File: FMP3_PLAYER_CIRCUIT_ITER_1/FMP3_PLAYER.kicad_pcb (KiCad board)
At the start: 4 copper layers, 114 x 39.5 mm, 47 parts, among them J1 USB_C_Receptacle_PowerOnly_6P, J2 AudioJack3, J3 ISP, Q1 PMOS, Q2 PMOS, SW1 SW_L, SW2 SW_D, SW3 SW_R, SW4 SW_U, SW5 SW_SPDT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

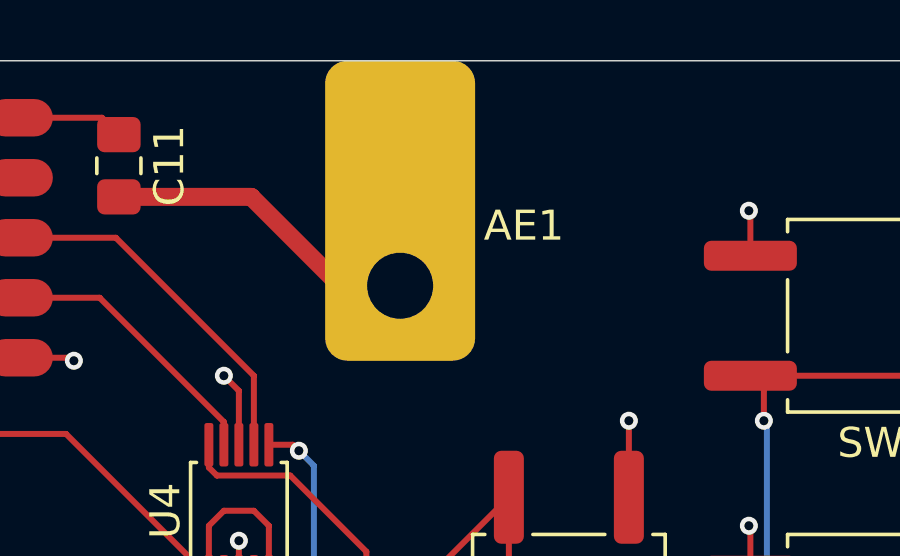
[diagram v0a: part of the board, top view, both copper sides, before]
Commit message: Started a new iteration cause 4 layer to expensive
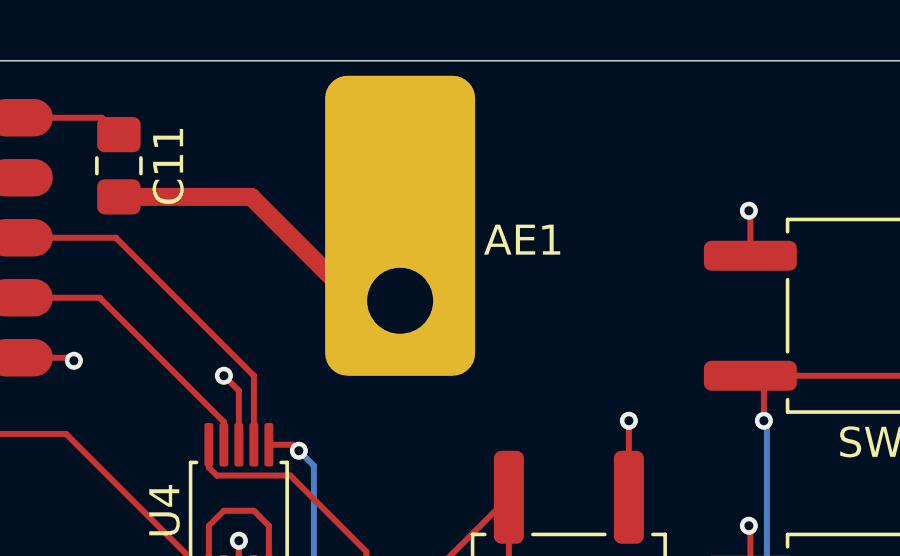
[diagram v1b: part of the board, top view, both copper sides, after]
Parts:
- moved AE1 0.50 mm to (162.9, 42.0)
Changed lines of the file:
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@@
 			(outputformat 1)
 			(mirror no)
-			(drillshape 1)
+			(drillshape 0)
 			(scaleselection 1)
-			(outputdirectory "")
+			(outputdirectory "../../../../Downloads/")
 		)
 	)
@@
 	(footprint "Custom_footprints:FM_Antenna_Mount"
 		(layer "F.Cu")
-		(at 162.875 41.5 180)
+		(at 162.875 42 180)
 		(property "Reference" "AE1"
 			(at -1.625 -0.5 0)
